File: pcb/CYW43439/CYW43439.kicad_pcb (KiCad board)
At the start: 2 copper layers, 29.9 x 22 mm, 31 parts, among them J1 GPIOs, J2 SPI, J3 Power, U1 CYW43439KUBGT, Y1 Crystal

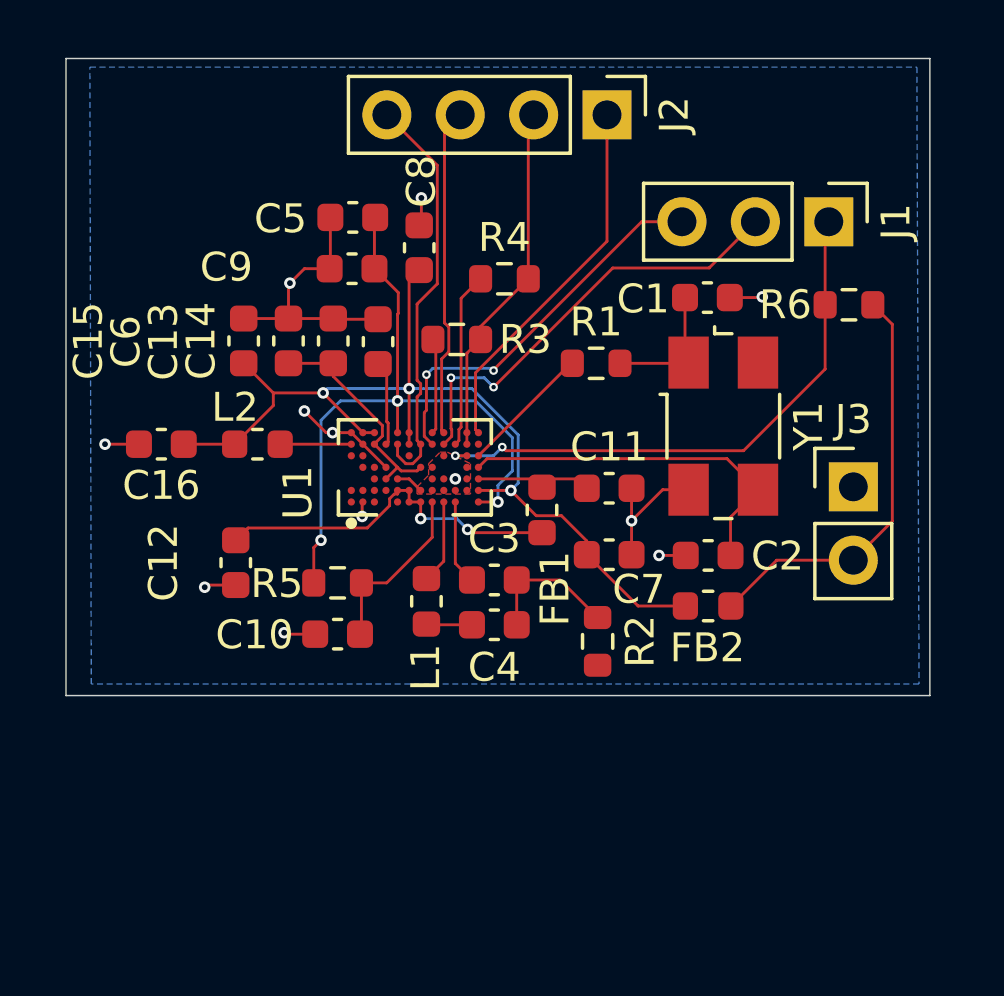
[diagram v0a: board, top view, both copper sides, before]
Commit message: [pcb] move rev2 into dedicated folder + start new rev
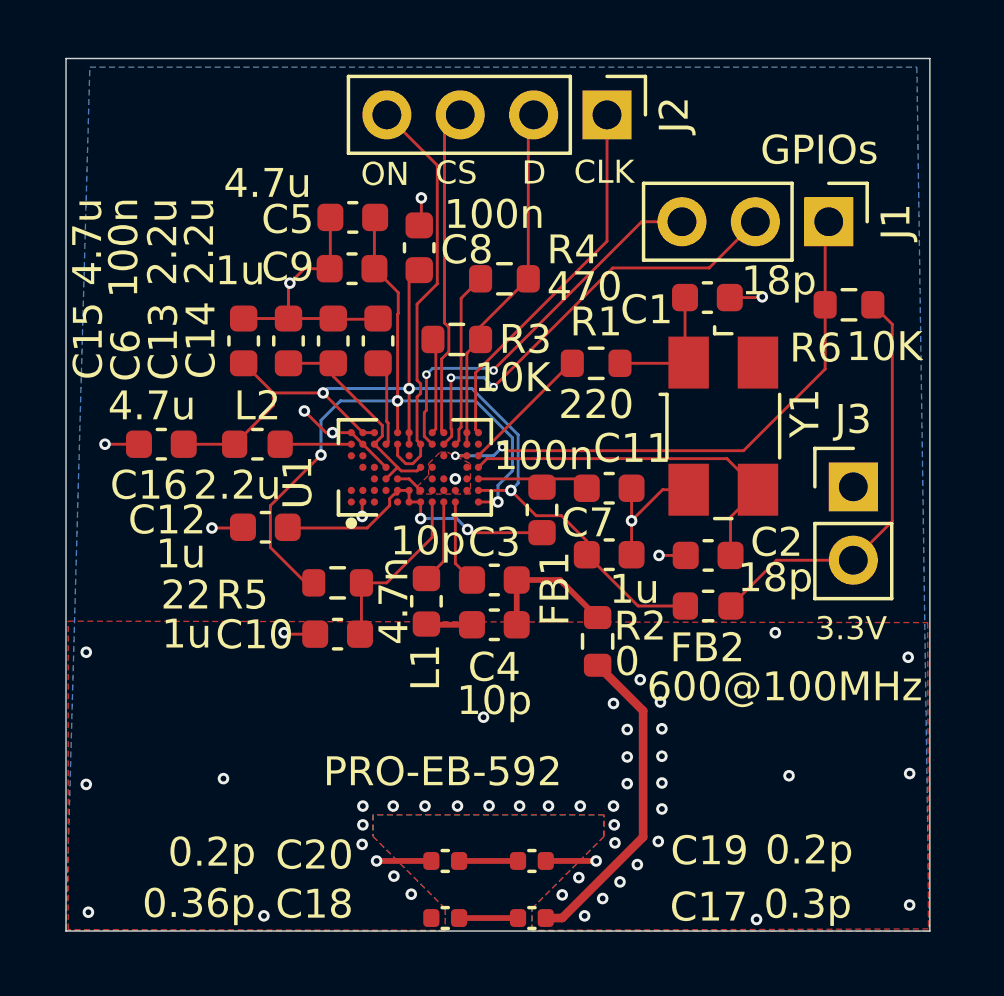
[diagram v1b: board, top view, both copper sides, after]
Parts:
- added C17: 0.3p, Capacitor_SMD:C_0402_1005Metric, F.Cu at (141.8, 111.9)
- added C18: 0.36p, Capacitor_SMD:C_0402_1005Metric, F.Cu at (138.8, 111.9)
- added C19: 0.2p, Capacitor_SMD:C_0402_1005Metric, F.Cu at (141.8, 109.9)
- added C20: 0.2p, Capacitor_SMD:C_0402_1005Metric, F.Cu at (138.8, 109.9)
- moved C12 1.60 mm to (132.6, 98.4), turned to 180 degrees
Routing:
- net ANTENNA: track 0.00 -> 11.1 mm
- net GND: track 25.5 -> 29.1 mm, vias 12 -> 58
- net Net-(C19-Pad2): track 0.00 -> 2.04 mm
- net Net-(C17-Pad2): track 0.00 -> 2.04 mm
- net Net-(U1-BTFM_PLL_VDD): track 12.7 -> 10.7 mm
- net VOUT_3P3: track 24.1 -> 25.5 mm
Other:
- board size 29.9 x 22 mm -> 29.9 x 30.2 mm
- board text added: "3.3V"
- board text added: "CLK"
- board text added: "CS"
- board text added: "D"
- board text added: "ON"
- board text added: "PRO-EB-592"
